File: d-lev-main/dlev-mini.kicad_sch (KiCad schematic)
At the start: 41 parts, among them J1 IO_BOARD, J3 S8B-PH-SM4-TB, J4 S8B-PH-SM4-TB, J6 S6B-PH-SM4-TB, Q3 BSS138, Q4 BSS138, Q5 BSS138, U2 AMS1117-3.3, U4 25LCxxx

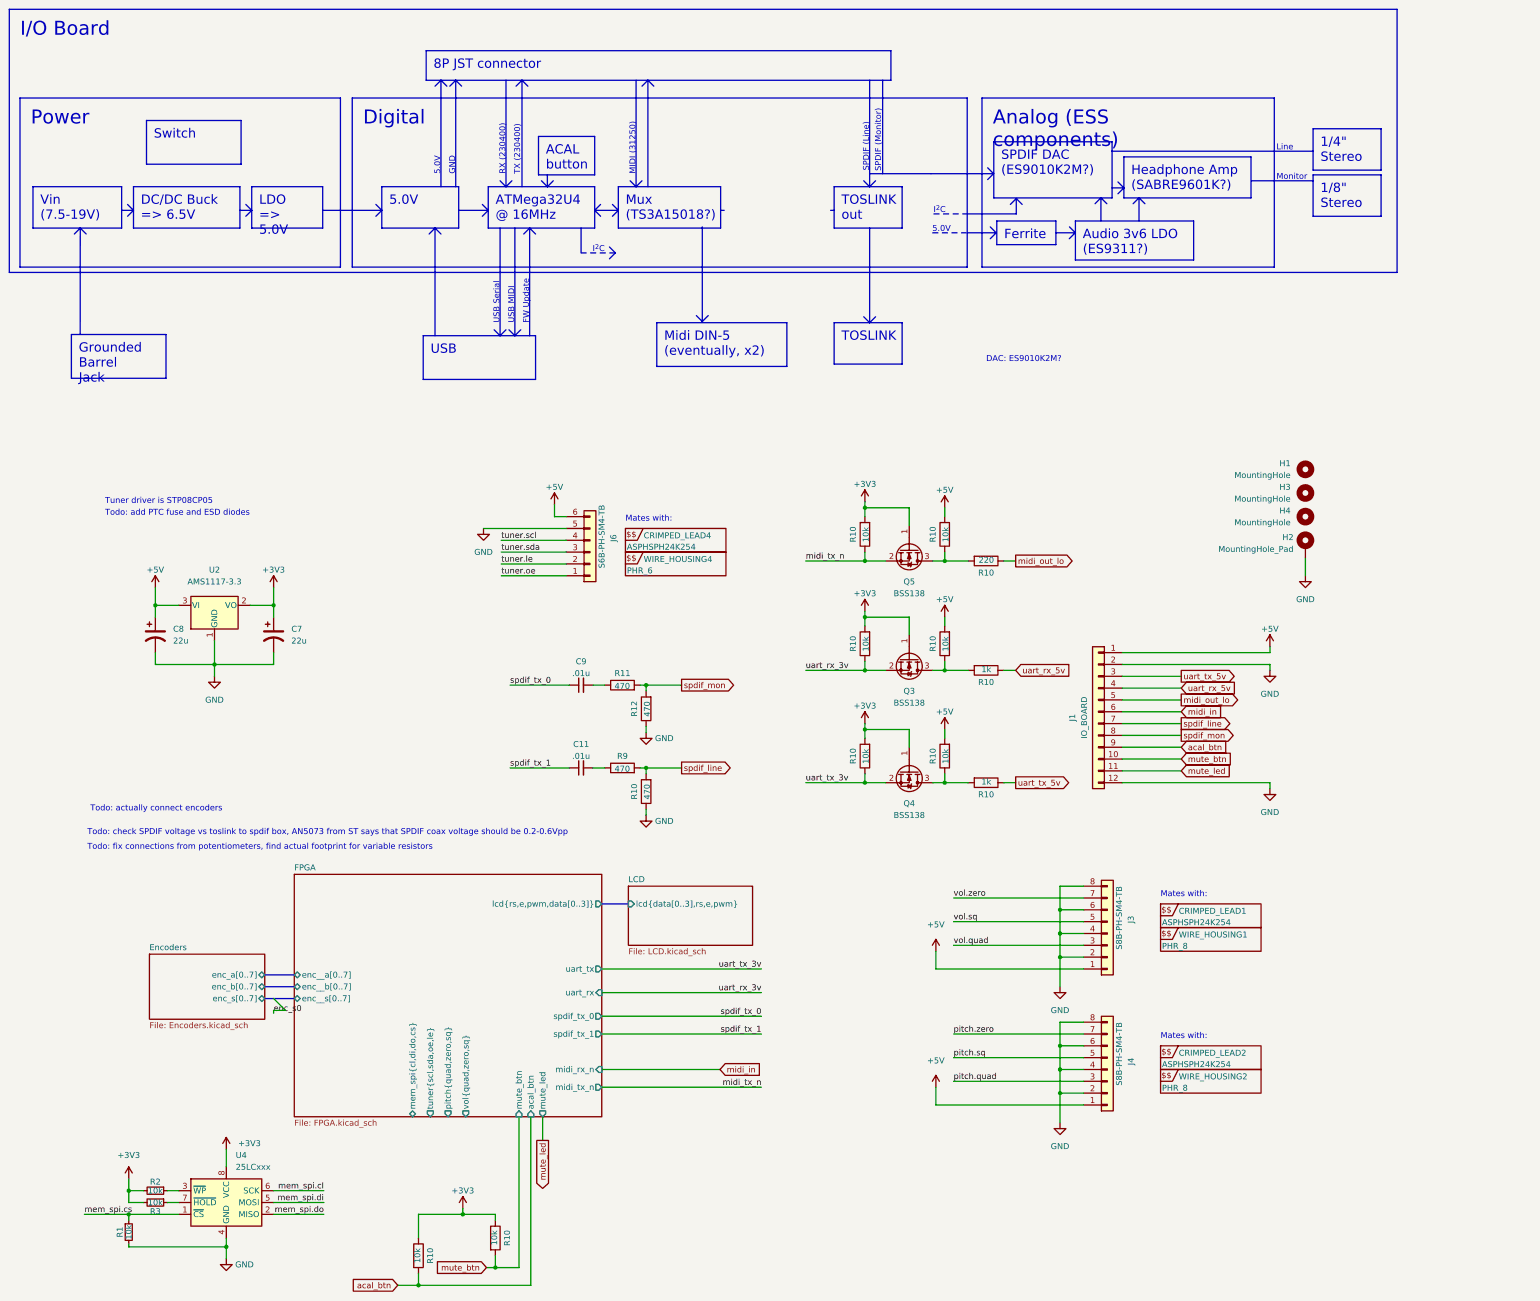
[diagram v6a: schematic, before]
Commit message: Small changes to 3D models and footprints; fixed bus routing of encoder signals
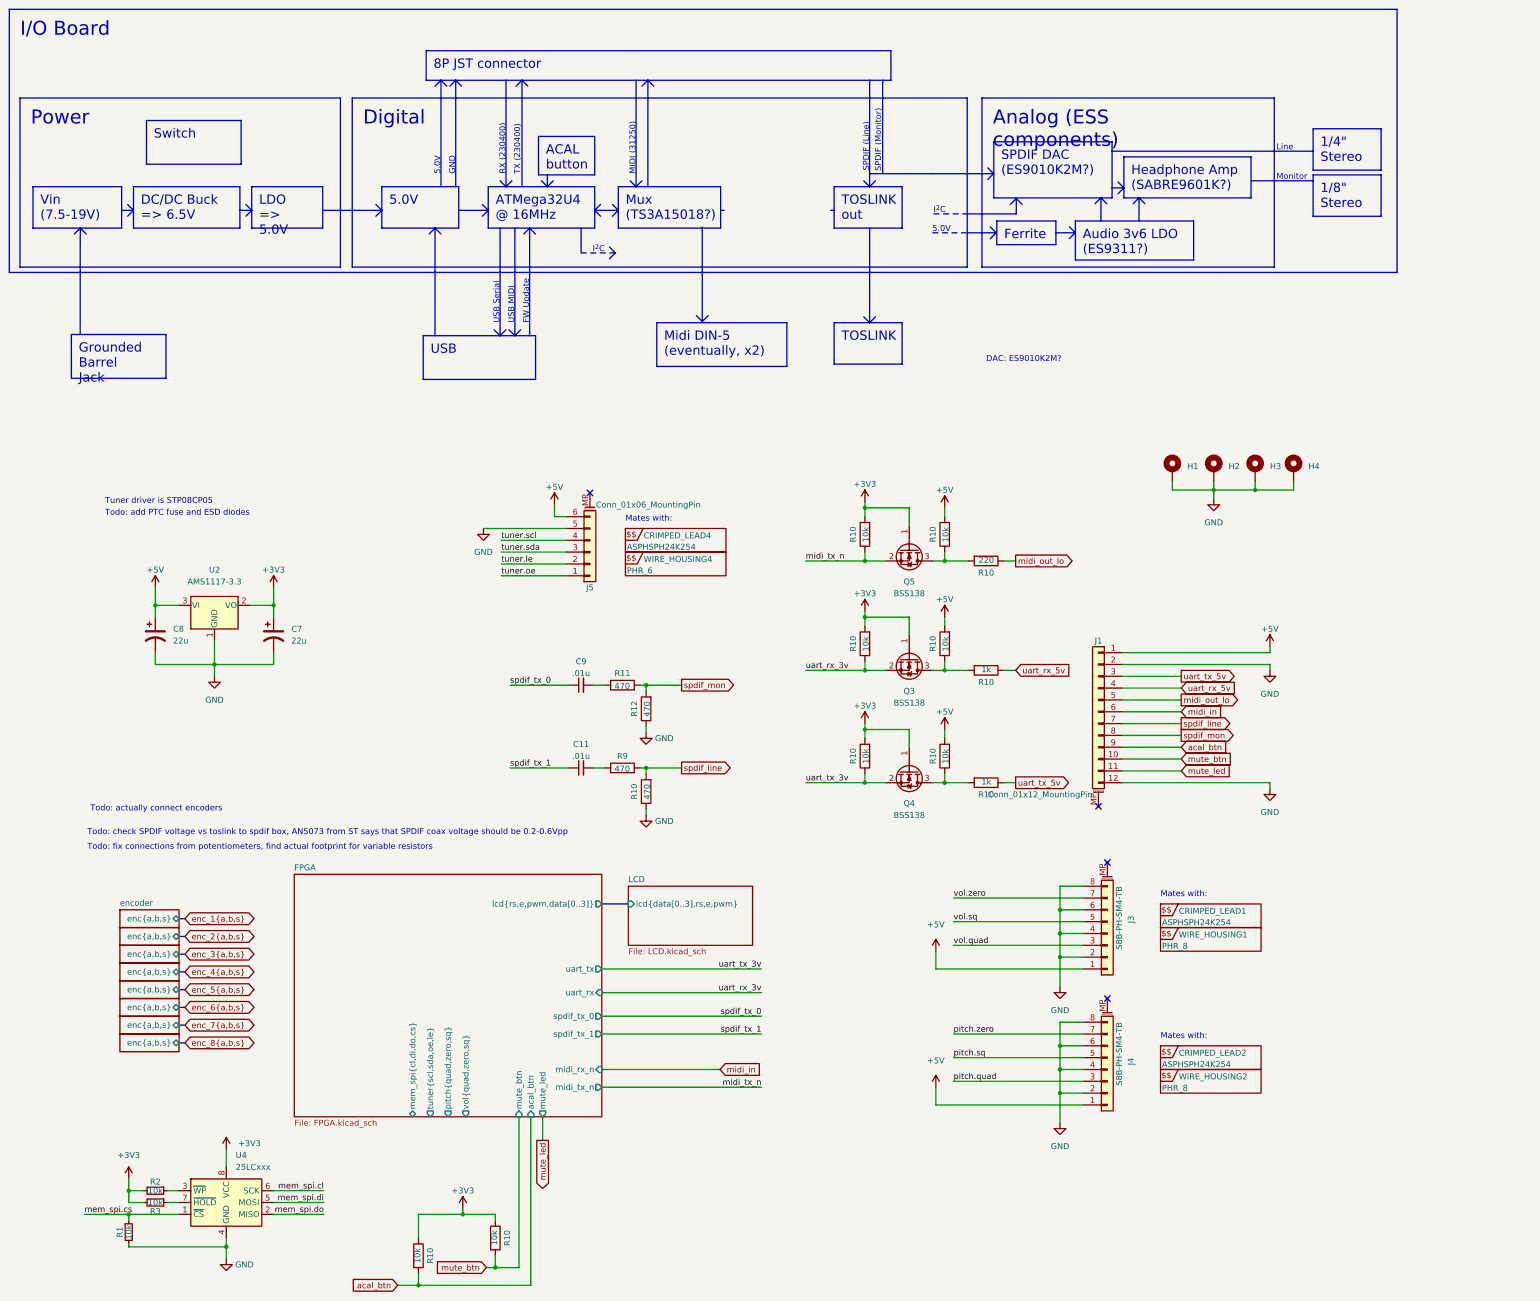
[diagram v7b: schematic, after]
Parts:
- H1, H3, H4: value MountingHole -> MountingHole_Pad; symbol Mechanical:MountingHole -> Mechanical:MountingHole_Pad
- J1: value IO_BOARD -> Conn_01x12_MountingPin; symbol Connector_Generic:Conn_01x12 -> Connector_Generic_MountingPin:Conn_01x12_MountingPin
- J3, J4: symbol Connector_Generic:Conn_01x08 -> Connector_Generic_MountingPin:Conn_01x08_MountingPin
- J5: renamed from J6; value S6B-PH-SM4-TB -> Conn_01x06_MountingPin; symbol Connector_Generic:Conn_01x06 -> Connector_Generic_MountingPin:Conn_01x06_MountingPin
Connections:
- net GND: now also H1.1, H3.1, H4.1
- no-connect marks 0 -> 4
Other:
- removed sheet Encoders
- added sheet encoder (SingleEncoder.kicad_sch)
- added sheet encoder1 (SingleEncoder.kicad_sch)
- added sheet encoder2 (SingleEncoder.kicad_sch)
- added sheet encoder3 (SingleEncoder.kicad_sch)
- added sheet encoder4 (SingleEncoder.kicad_sch)
- added sheet encoder5 (SingleEncoder.kicad_sch)
- added sheet encoder6 (SingleEncoder.kicad_sch)
- added sheet encoder7 (SingleEncoder.kicad_sch)
- sheet FPGA ports: added none; removed enc__a[0..7], enc__b[0..7], enc__s[0..7]
- moved on the sheet: H2
